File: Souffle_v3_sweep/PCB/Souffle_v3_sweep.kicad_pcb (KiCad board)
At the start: 2 copper layers, 137.2 x 114.5 mm, 82 parts, among them J1 LED, J2 4PIN, J3 OLED, SW1 SW_PUSH, SW10 SW_PUSH, SW11 SW_PUSH, SW12 SW_PUSH, SW13 SW_PUSH, SW14 SW_PUSH, SW15 SW_PUSH, SW16 SW_PUSH, SW17 SW_PUSH, SW18 SW_PUSH, SW19 SW_PUSH, SW2 SW_PUSH, SW20 SW_PUSH, SW21 SW_PUSH, SW22 SW_PUSH, SW23 SW_PUSH, SW24 SW_PUSH, SW25 SW_PUSH, SW25b1 RotaryEncoder_Switch, SW26 SW_PUSH, SW27 SW_PUSH, SW28 SW_PUSH, SW29 SW_PUSH, SW3 SW_PUSH, SW30 SW_PUSH, SW31 SW_SPDT, SW4 SW_PUSH, SW5 SW_PUSH, SW6 SW_PUSH, SW7 SW_PUSH, SW8 SW_PUSH, SW9 SW_PUSH, U1 ProMicro

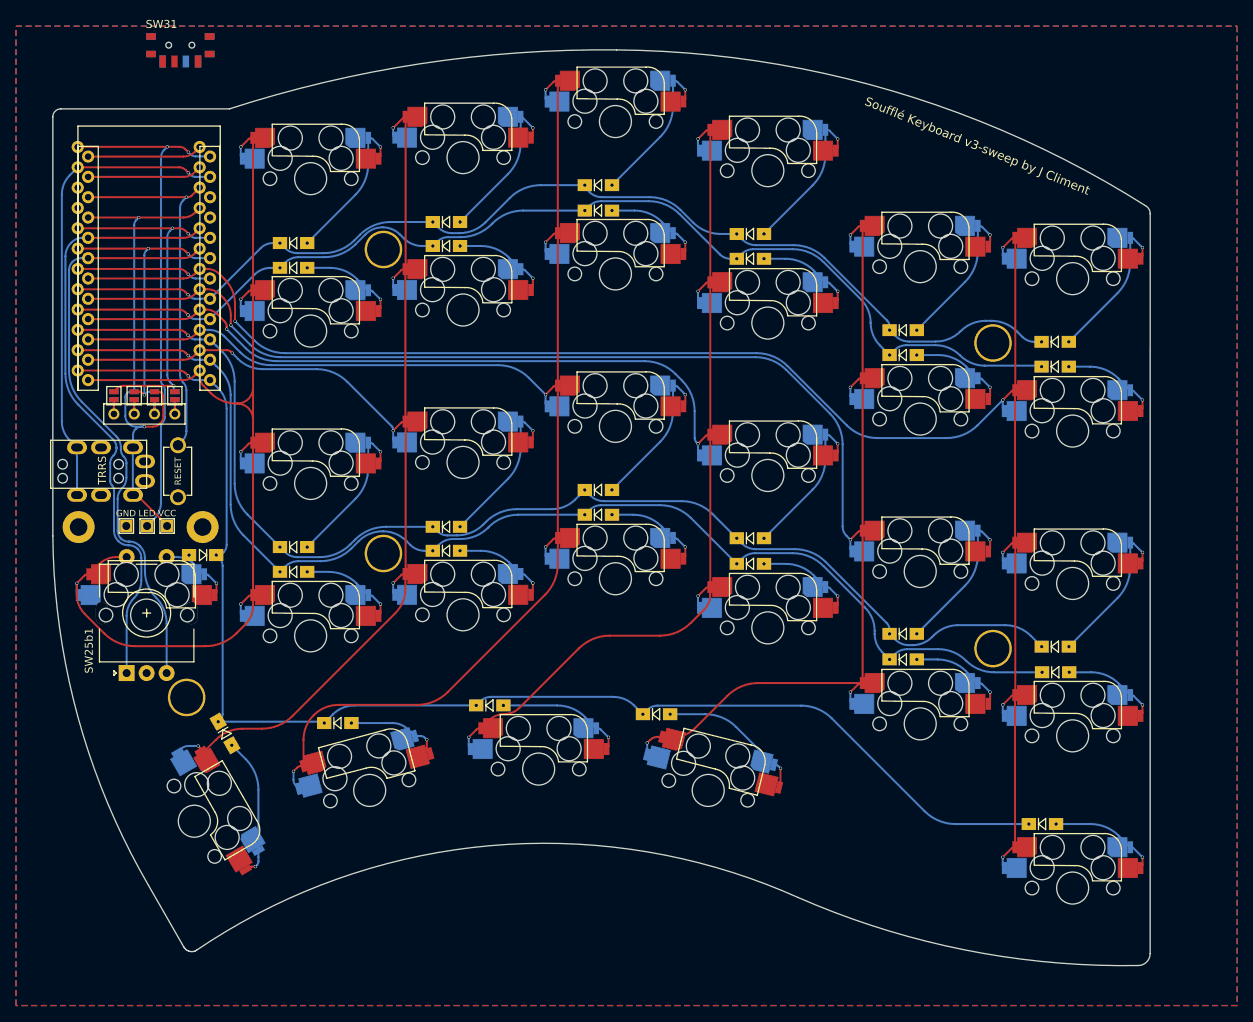
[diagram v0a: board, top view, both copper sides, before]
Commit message: Added battery pins and power switch for nice!nano option.
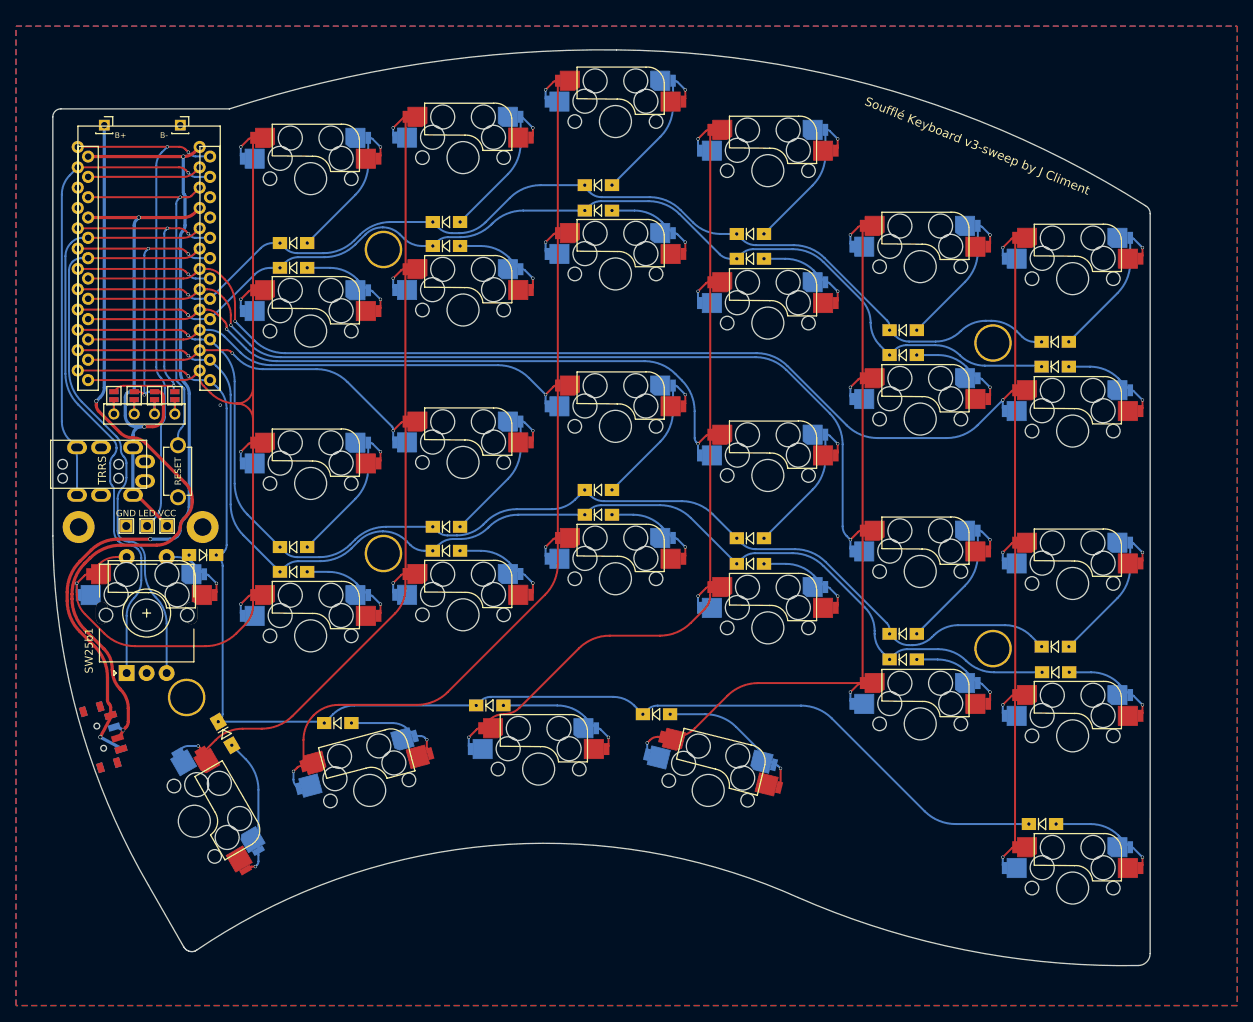
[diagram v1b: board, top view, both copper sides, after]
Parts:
- added J4: Conn_01x01_Female, Connector_PinSocket_2.00mm:PinSocket_1x01_P2.00mm_Vertical, F.Cu at (89.8, 38.7)
- added J5: Conn_01x01_Female, Connector_PinSocket_2.00mm:PinSocket_1x01_P2.00mm_Vertical, F.Cu at (80.3, 38.7)
- moved SW31 87.1 mm to (79.8, 115.2), turned to -73 degrees
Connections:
- U1 pad 24: unconnected-(U1-Pad24) -> RAW
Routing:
- net RAW: track 0.00 -> 103.2 mm, vias 0 -> 3
- net BAT: track 0.00 -> 96.4 mm, vias 0 -> 2
- net unconnected-(U1-Pad24): track 14.3 -> 0.00 mm
- net GND: vias 0 -> 1
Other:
- board text added: "B+"
- board text added: "B-"

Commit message: Small track changes.
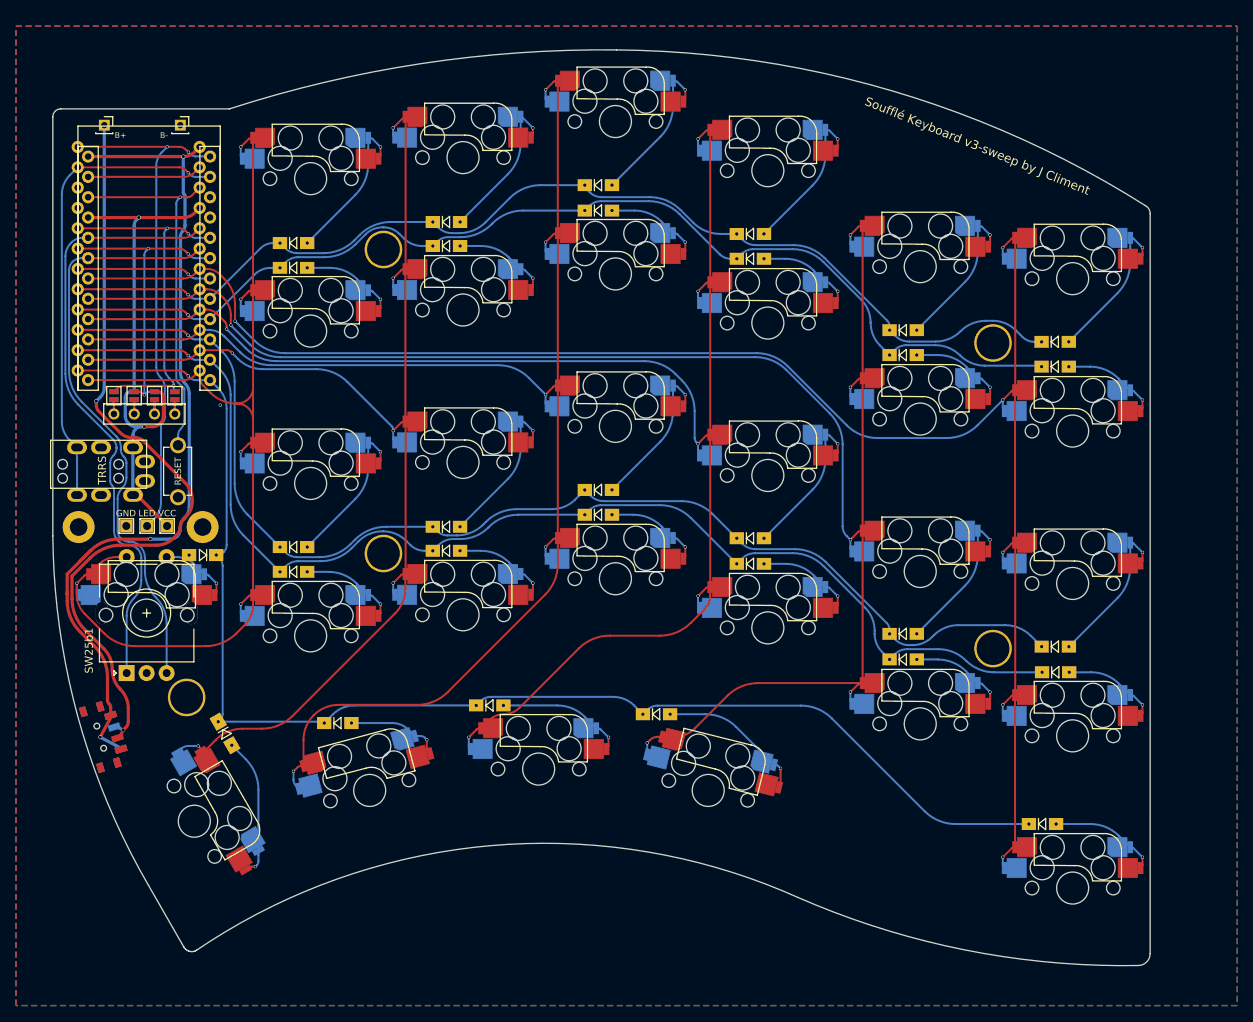
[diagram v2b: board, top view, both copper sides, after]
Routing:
- net RAW: track 103.2 -> 105.7 mm

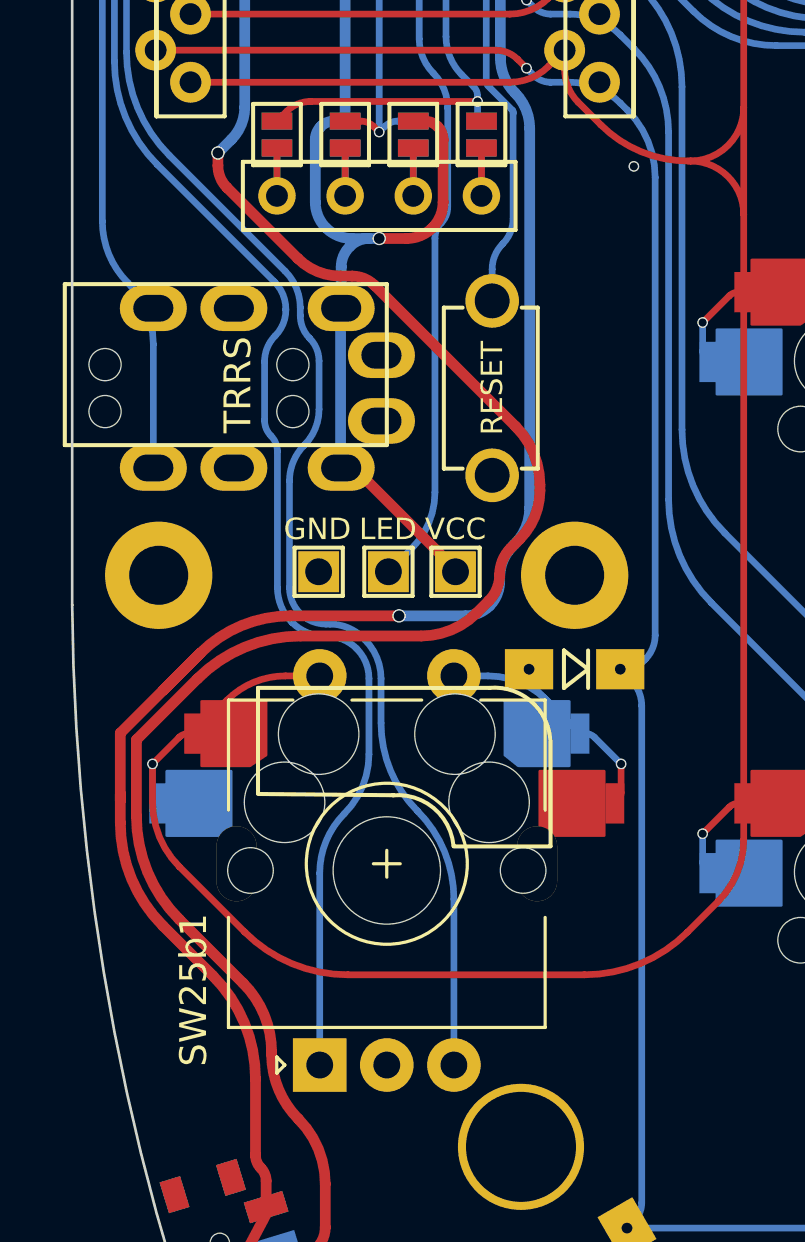
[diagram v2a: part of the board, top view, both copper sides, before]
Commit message: Fixed error in GND not connected on the right side of the OLED pads, and other small cleanups.
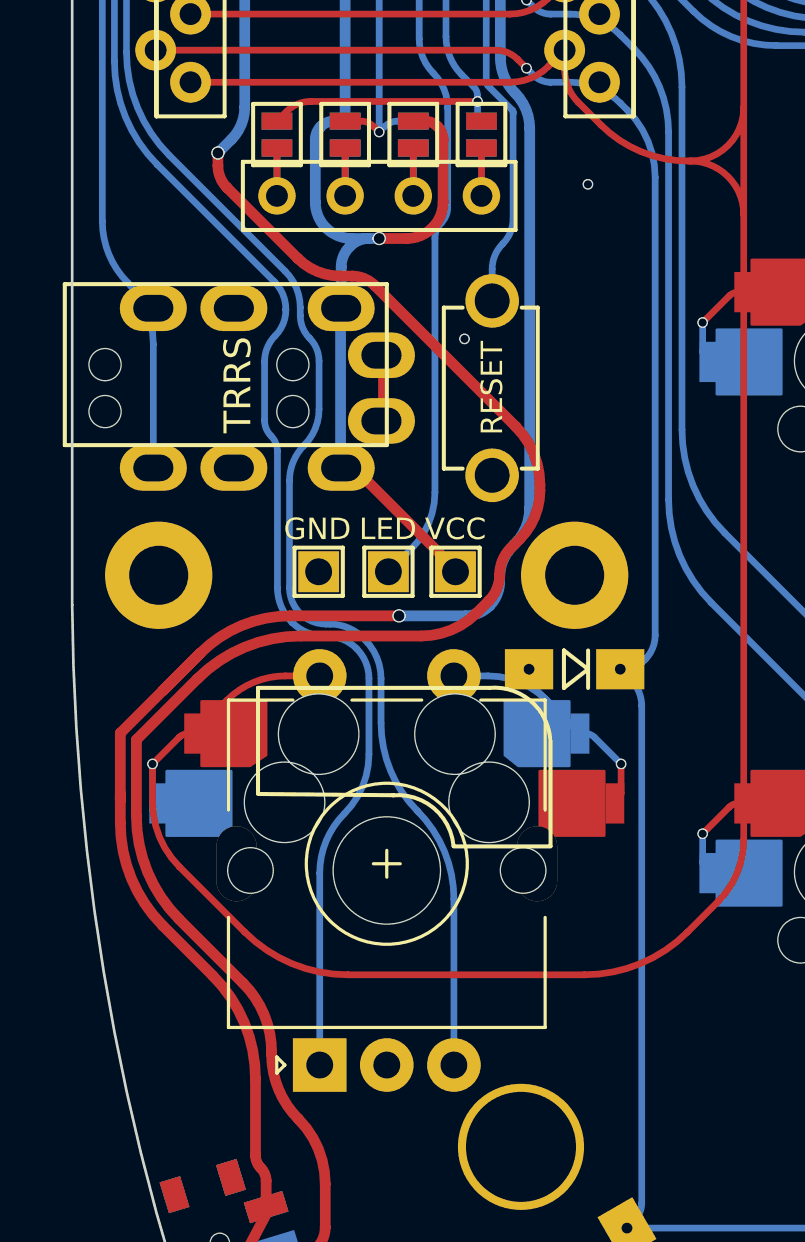
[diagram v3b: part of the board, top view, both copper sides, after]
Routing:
- net unconnected-(J2-Pad4): track 0.00 -> 2.45 mm
- net GND: vias 1 -> 2

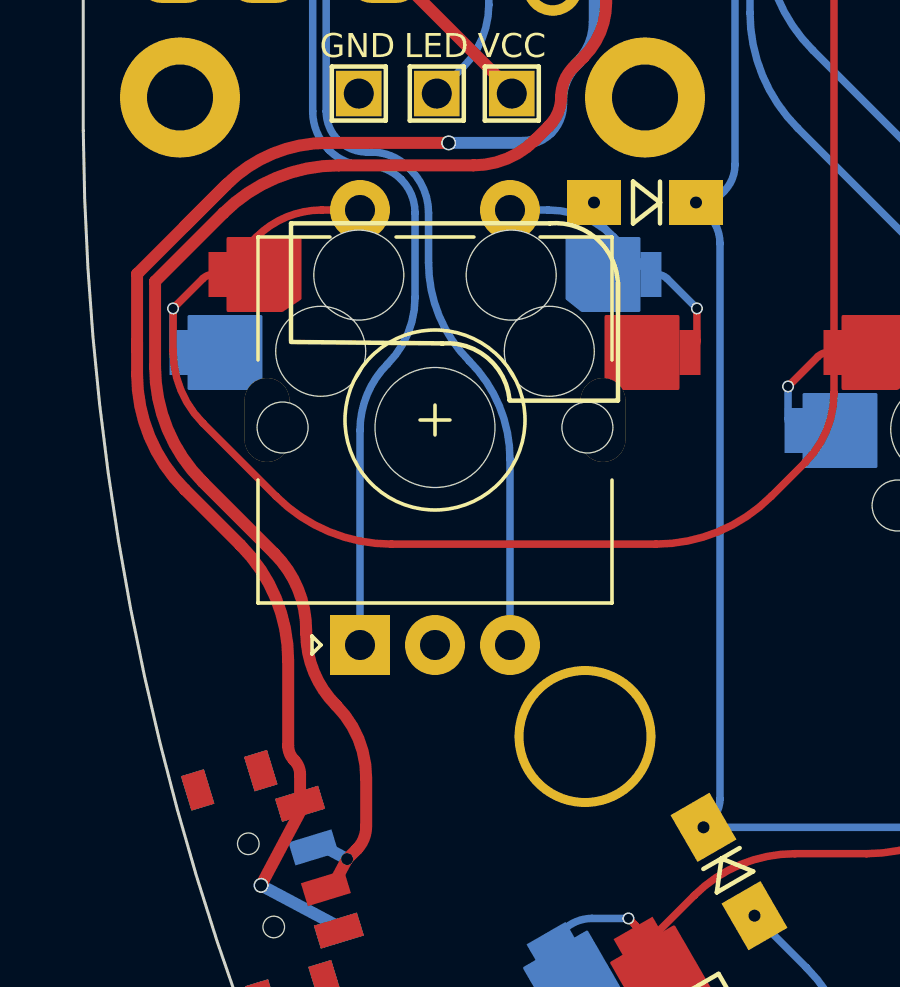
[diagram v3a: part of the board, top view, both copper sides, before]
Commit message: Corrected PCB with displaced encoder.
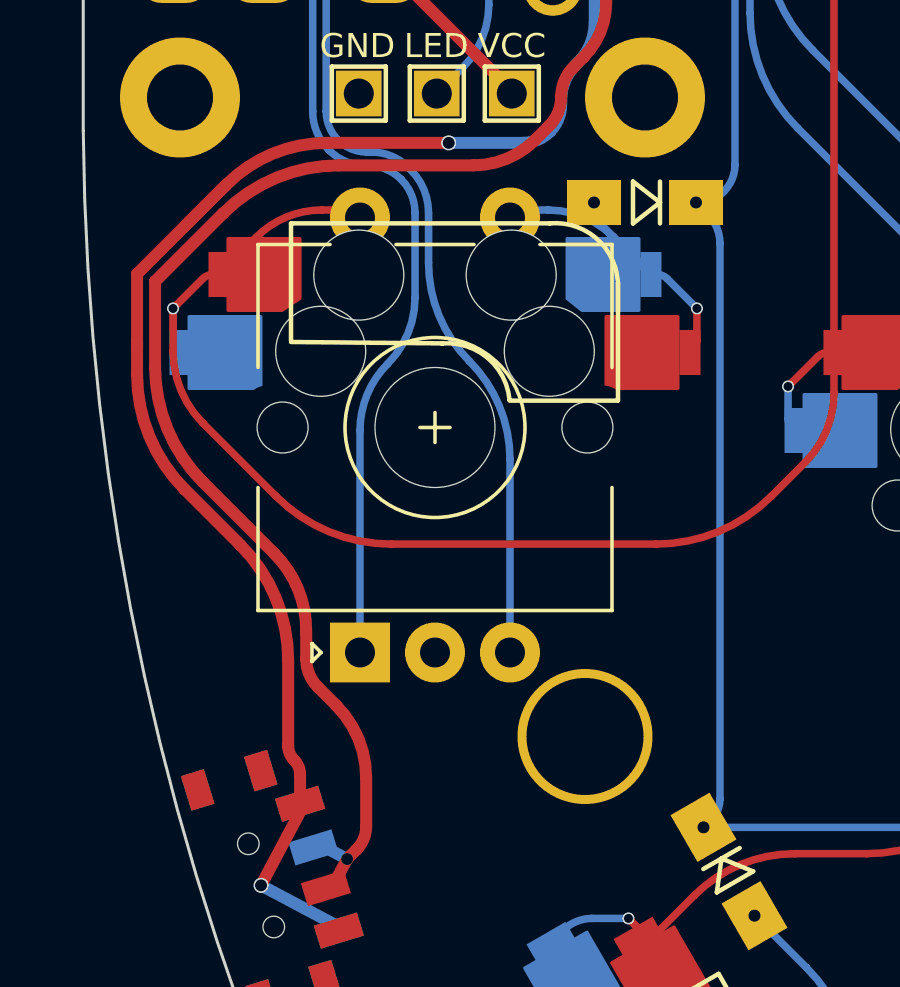
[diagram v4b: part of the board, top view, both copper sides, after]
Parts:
- moved SW25b1 0.25 mm to (83.1, 107.5)
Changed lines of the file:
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@@
       (effects (font (size 0.8 0.8) (thickness 0.15)))
     )
-    (fp_text value "Conn_01x01_Female" (at 0 2.5) (layer "F.Fab")
+    (fp_text value "Conn_01x01_Female" (at 0 2.5) (layer "F.Fab") hide
       (effects (font (size 1 1) (thickness 0.15)))
     )
@@
   )
   (footprint "Rotary_Encoder:RotaryEncoder_Alps_EC11E-Switch_Vertical_H20mm" (layer "F.Cu")
-    (at 83.134 107.223139 90)
+    (at 83.134 107.473139 90)
     (descr "Alps rotary encoder, EC12E... with switch, vertical shaft, http://www.alps.com/prod/info/E/HTML/Encoder/Incremental/EC11/EC11E15204A3.html")
     (tags "rotary encoder")
@@
       (effects (font (size 1 1) (thickness 0.15)))
     )
-    (fp_text value "RotaryEncoder_Switch" (at 7.5 10.4 90) (layer "F.Fab")
+    (fp_text value "RotaryEncoder_Switch" (at 7.5 10.4 90) (layer "F.Fab") hide
       (effects (font (size 1 1) (thickness 0.15)))
     )
@@
     (fp_line (start 4.5 2.5) (end 10.5 2.5) (layer "F.Fab") (width 0.12))
     (fp_circle (center 7.5 2.5) (end 10.5 2.5) (layer "F.Fab") (width 0.12) (fill none))
+    (pad "" np_thru_hole oval (at 7.5 8.1 90) (size 2.8 1.5) (drill oval 2.8 1.5) (layers F&B.Cu *.Mask))
+    (pad "" np_thru_hole oval (at 7.5 -3.1 90) (size 2.8 1.5) (drill oval 2.8 1.5) (layers F&B.Cu *.Mask))
     (pad "A" thru_hole rect (at 0 0 90) (size 2 2) (drill 1) (layers *.Cu *.Mask)
       (net 54 "ENCA") (pinfunction "A") (pintype "passive"))
@@
     (pad "C" thru_hole circle (at 0 2.5 90) (size 2 2) (drill 1) (layers *.Cu *.Mask)
       (net 38 "GND") (pinfunction "C") (pintype "passive"))
-    (pad "MP" thru_hole oval (at 7.5 8.1 90) (size 2.8 1.5) (drill oval 2.8 1.5) (layers *.Cu *.Mask))
-    (pad "MP" thru_hole oval (at 7.5 -3.1 90) (size 2.8 1.5) (drill oval 2.8 1.5) (layers *.Cu *.Mask))
     (pad "S1" thru_hole circle (at 14.5 5 90) (size 2 2) (drill 1) (layers *.Cu *.Mask)
       (net 30 "SW25B") (pinfunction "S1") (pintype "passive"))
@@
       (effects (font (size 0.8 0.8) (thickness 0.15)))
     )
-    (fp_text value "Conn_01x01_Female" (at 0 2.5) (layer "F.Fab")
+    (fp_text value "Conn_01x01_Female" (at 0 2.5) (layer "F.Fab") hide
       (effects (font (size 1 1) (thickness 0.15)))
     )
@@
       (effects (font (size 0.29972 0.29972) (thickness 0.0762)))
     )
-    (pad "" thru_hole circle locked (at 0 0 180) (size 4.7 4.7) (drill 4.1) (layers *.Cu *.Mask "Dwgs.User")
+    (pad "" thru_hole circle locked (at 0 0 180) (size 4.5 4.5) (drill 3.9) (layers *.Cu *.Mask "Dwgs.User")
       (clearance 0.3))
   )
@@
   (segment (start 88.98225 90.377639) (end 89.434772 89.925116) (width 0.4) (layer "F.Cu") (net 58))
   (segment (start 82.704057 114.358524) (end 83.022153 114.040427) (width 0.4) (layer "F.Cu") (net 58))
+  (segment (start 81.34025 106.821425) (end 81.340256 107.684813) (width 0.4) (layer "F.Cu") (net 58))
   (segment (start 90.442067 83.43415) (end 85.175112 78.167195) (width 0.4) (layer "F.Cu") (net 58))
   (segment (start 83.902646 77.823139) (end 84.344536 77.823149) (width 0.4) (layer "F.Cu") (net 58))
   (segment (start 81.34025 106.821425) (end 81.34025 106.735639) (width 0.4) (layer "F.Cu") (net 58))
   (segment (start 79.34025 73.712396) (end 79.34025 73.235639) (width 0.4) (layer "F.Cu") (net 58))
+  (segment (start 82.34025 109.235639) (end 81.729757 108.625144) (width 0.4) (layer "F.Cu") (net 58))
   (segment (start 83.34025 113.272474) (end 83.34025 111.649852) (width 0.4) (layer "F.Cu") (net 58))
   (segment (start 76.30275 97.944175) (end 76.30275 95.104388) (width 0.4) (layer "F.Cu") (net 58))
@@
   (arc (start 78.577706 92.829431) (mid 80.343072 91.649852) (end 82.425463 91.235639) (width 0.4) (layer "F.Cu") (net 58))
   (arc (start 91.34025 85.602554) (mid 91.106819 84.429022) (end 90.442067 83.43415) (width 0.4) (layer "F.Cu") (net 58))
-  (arc (start 82.34025 109.235639) (mid 81.600141 108.127988) (end 81.34025 106.821425) (width 0.4) (layer "F.Cu") (net 58))
+  (arc (start 81.729757 108.625144) (mid 81.441486 108.193716) (end 81.340256 107.684813) (width 0.4) (layer "F.Cu") (net 58))
   (segment (start 81.944764 113.954802) (end 82.704057 114.358524) (width 0.4) (layer "B.Cu") (net 58))
   (segment (start 81.705663 113.93178) (end 81.581344 113.969789) (width 0.25) (layer "B.Cu") (net 58))
